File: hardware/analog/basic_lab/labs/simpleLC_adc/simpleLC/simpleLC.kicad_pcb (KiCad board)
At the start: 2 copper layers, 40.2 x 16.4 mm, 5 parts, among them J1 Conn_01x04_Male, J2 Conn_01x02_Male, Q2 BC547

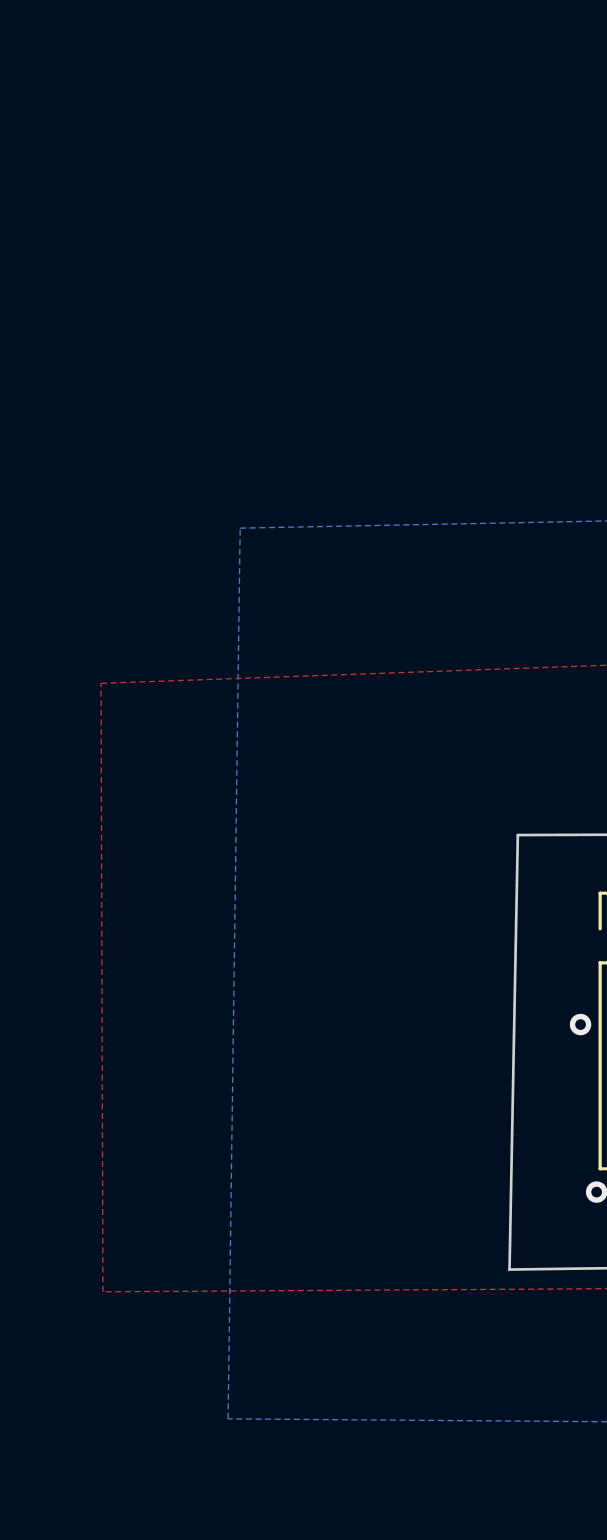
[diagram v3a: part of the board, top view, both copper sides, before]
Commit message: pwm => adc: started amplifier PCB
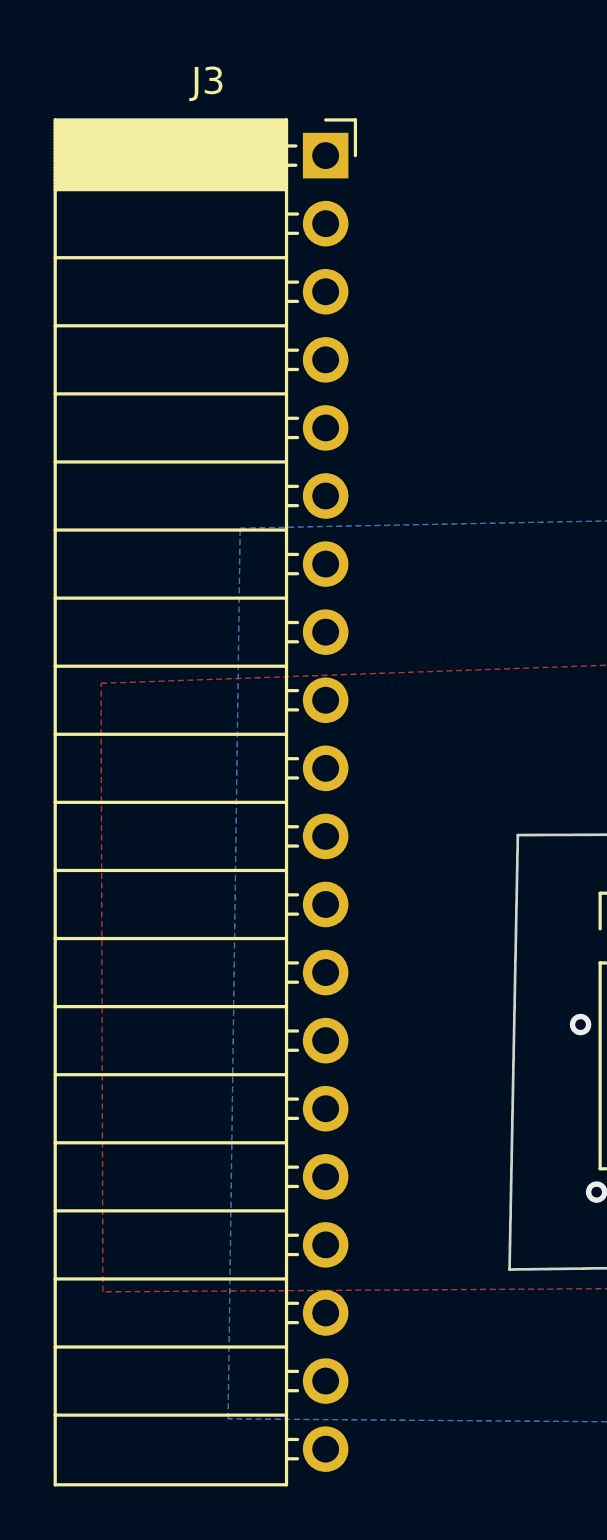
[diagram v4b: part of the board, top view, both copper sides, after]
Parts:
- added J3: Conn_01x20_Female, Connector_PinSocket_2.54mm:PinSocket_1x20_P2.54mm_Horizontal, F.Cu at (155.3, 60.8)

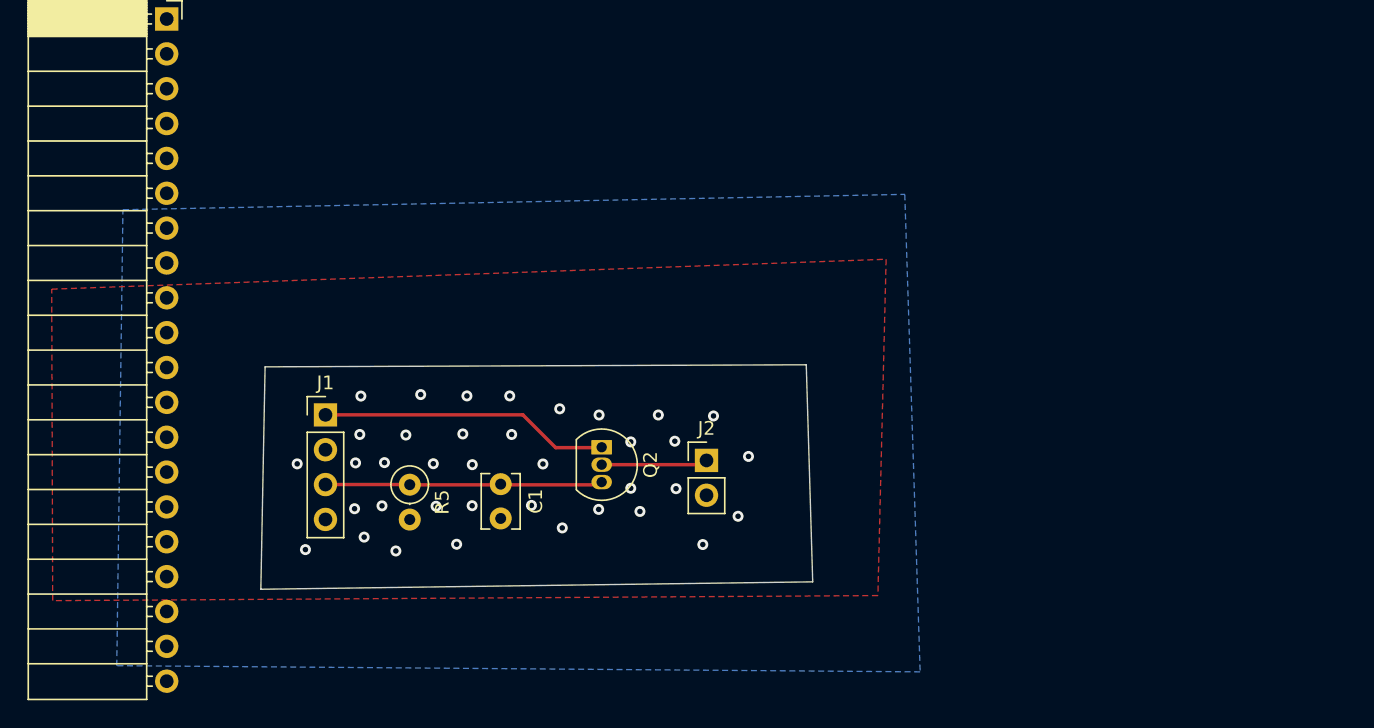
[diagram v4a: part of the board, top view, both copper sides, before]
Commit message: pwm => adc: started amplifier PCB
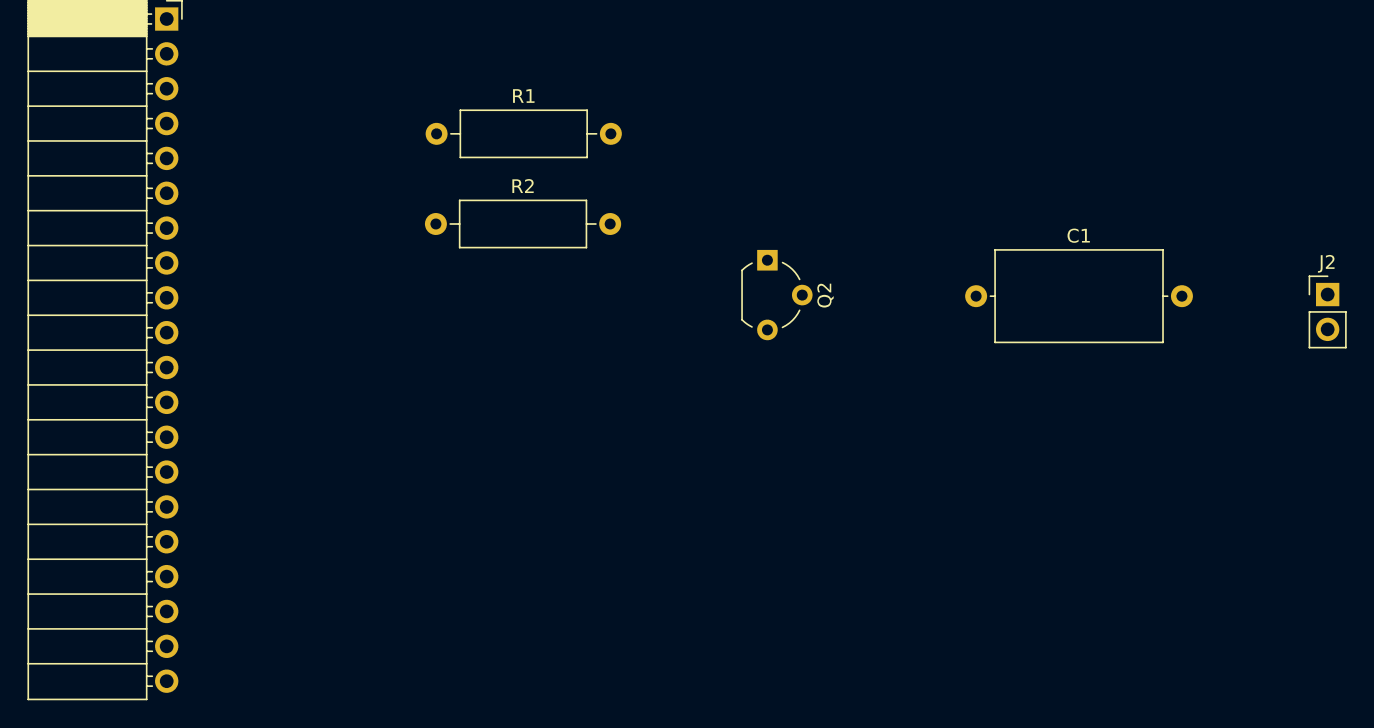
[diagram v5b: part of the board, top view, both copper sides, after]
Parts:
- removed J1: Conn_01x04_Male, Connector_PinHeader_2.54mm:PinHeader_1x04_P2.54mm_Vertical
- removed R5: R, Resistor_THT:R_Axial_DIN0207_L6.3mm_D2.5mm_P2.54mm_Vertical
- added R1: R, Resistor_THT:R_Axial_DIN0309_L9.0mm_D3.2mm_P12.70mm_Horizontal, F.Cu at (175.0, 69.2)
- added R2: R, Resistor_THT:R_Axial_DIN0309_L9.0mm_D3.2mm_P12.70mm_Horizontal, F.Cu at (175.0, 75.8)
- C1: footprint Capacitor_THT:C_Disc_D3.8mm_W2.6mm_P2.50mm -> Capacitor_THT:C_Axial_L12.0mm_D6.5mm_P15.00mm_Horizontal
- Q2: footprint Package_TO_SOT_THT:TO-92_Inline -> Package_TO_SOT_THT:TO-92_Wide
- moved J2 46.9 mm to (239.9, 80.9)
- moved C1 37.3 mm to (214.3, 81.0), turned to 0 degrees
- moved Q2 18.2 mm to (199.1, 78.4)
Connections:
- net Net-(J3-Pad11) renamed pwm
- C1 pad 1: aout -> Net-(C1-Pad1)
- C1 pad 2: GND -> Net-(C1-Pad2)
- J2 pad 1: Net-(J2-Pad1) -> Net-(C1-Pad2)
- J3 pad 12: Net-(J3-Pad12) -> adc
- J3 pad 18: Net-(J3-Pad18) -> GND
- J3 pad 19: Net-(J3-Pad19) -> +3V3
- J3 pad 20: Net-(J3-Pad20) -> GND
- Q2 pad 1: +3V3 -> adc
- Q2 pad 2: Net-(J2-Pad1) -> Net-(C1-Pad1)
- Q2 pad 3: aout -> GND
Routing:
- net +3V3: track 21.2 -> 0.00 mm
- net aout: track 20.2 -> 0.00 mm
- net Net-(J2-Pad1): track 7.84 -> 0.00 mm
- net GND: vias 37 -> 0
- removed copper zone on B.Cu, net GND
- removed copper zone on F.Cu, net GND
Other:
- board outline removed

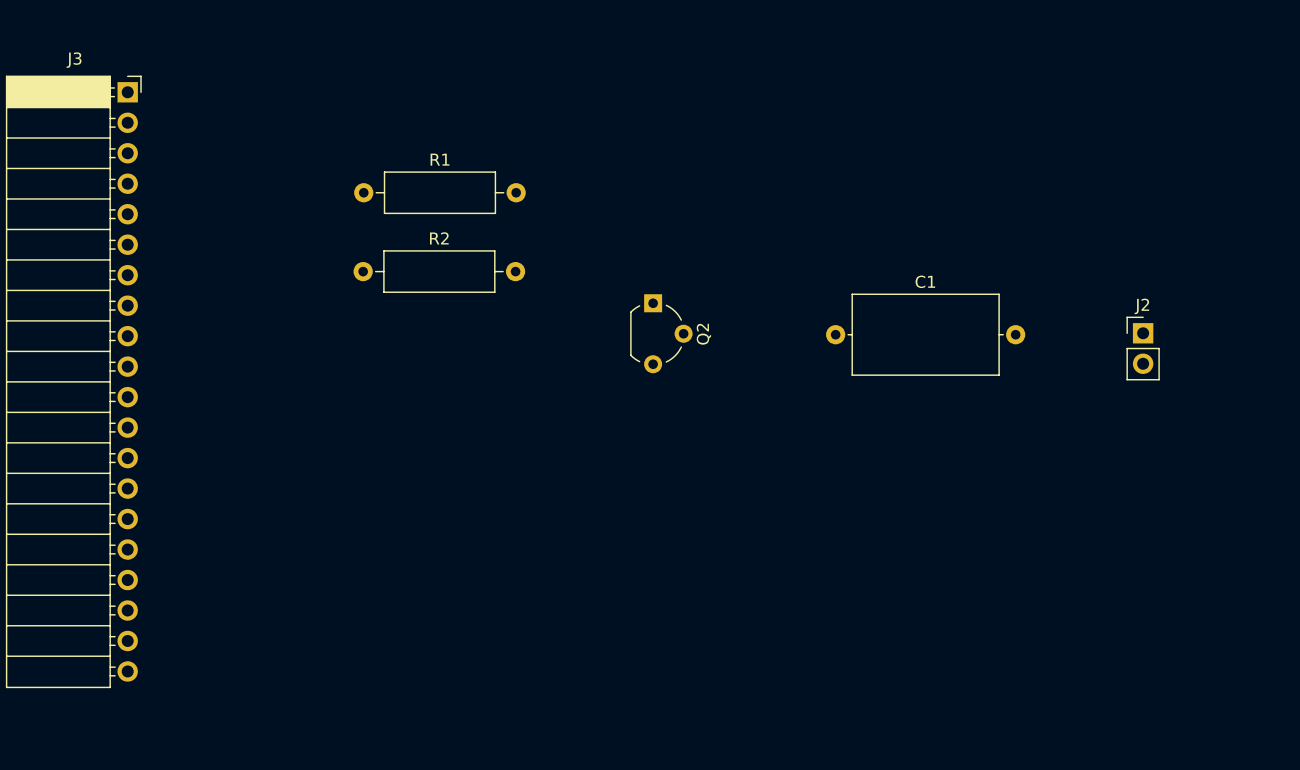
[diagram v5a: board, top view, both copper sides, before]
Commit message: pwm => adc: started amplifier PCB
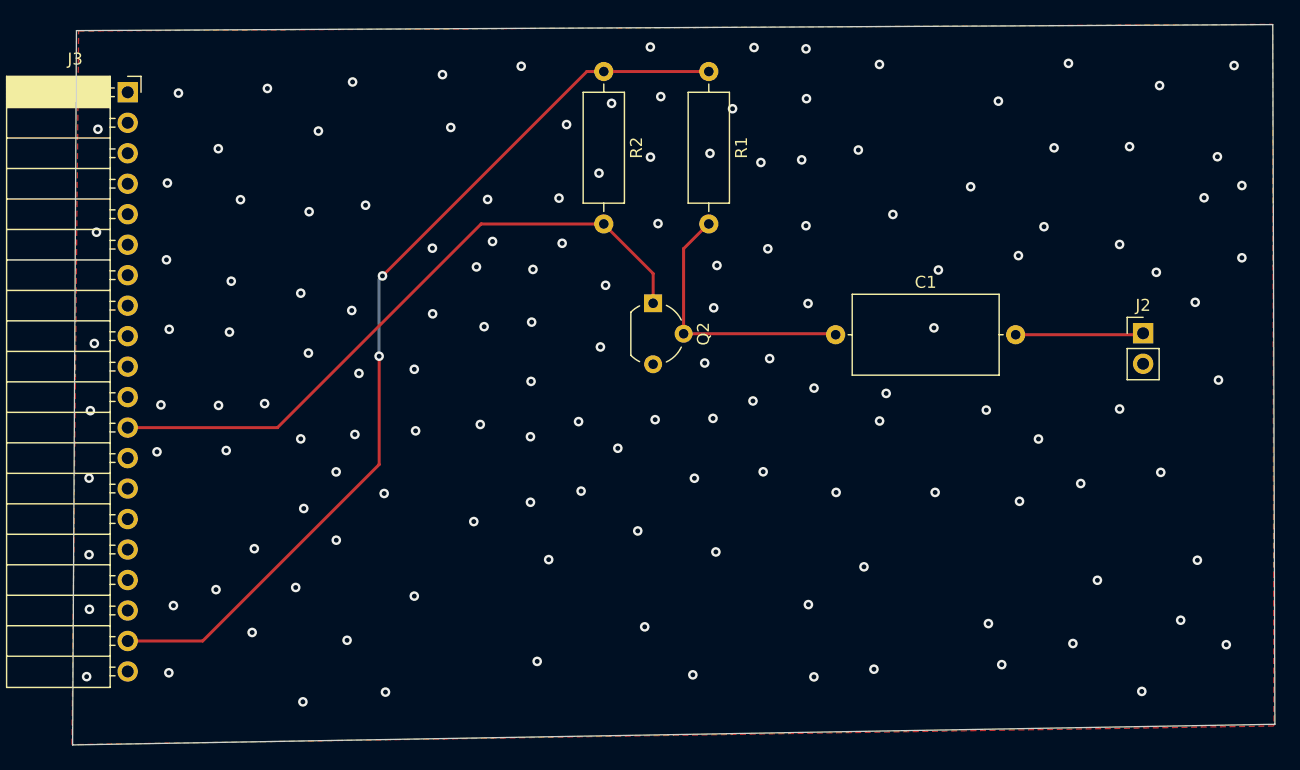
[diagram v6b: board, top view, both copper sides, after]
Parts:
- moved R1 30.5 mm to (203.8, 59.1), turned to 270 degrees
- moved R2 26.1 mm to (195.0, 59.1), turned to 270 degrees
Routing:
- net +3V3: track 0.00 -> 77.1 mm, vias 0 -> 2
- net adc: track 0.00 -> 55.0 mm
- net Net-(C1-Pad1): track 0.00 -> 22.6 mm
- net Net-(C1-Pad2): track 0.00 -> 10.6 mm
- net GND: vias 0 -> 148
- added copper zone on F.Cu, net GND
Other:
- board outline added: 100.2 x 60 mm

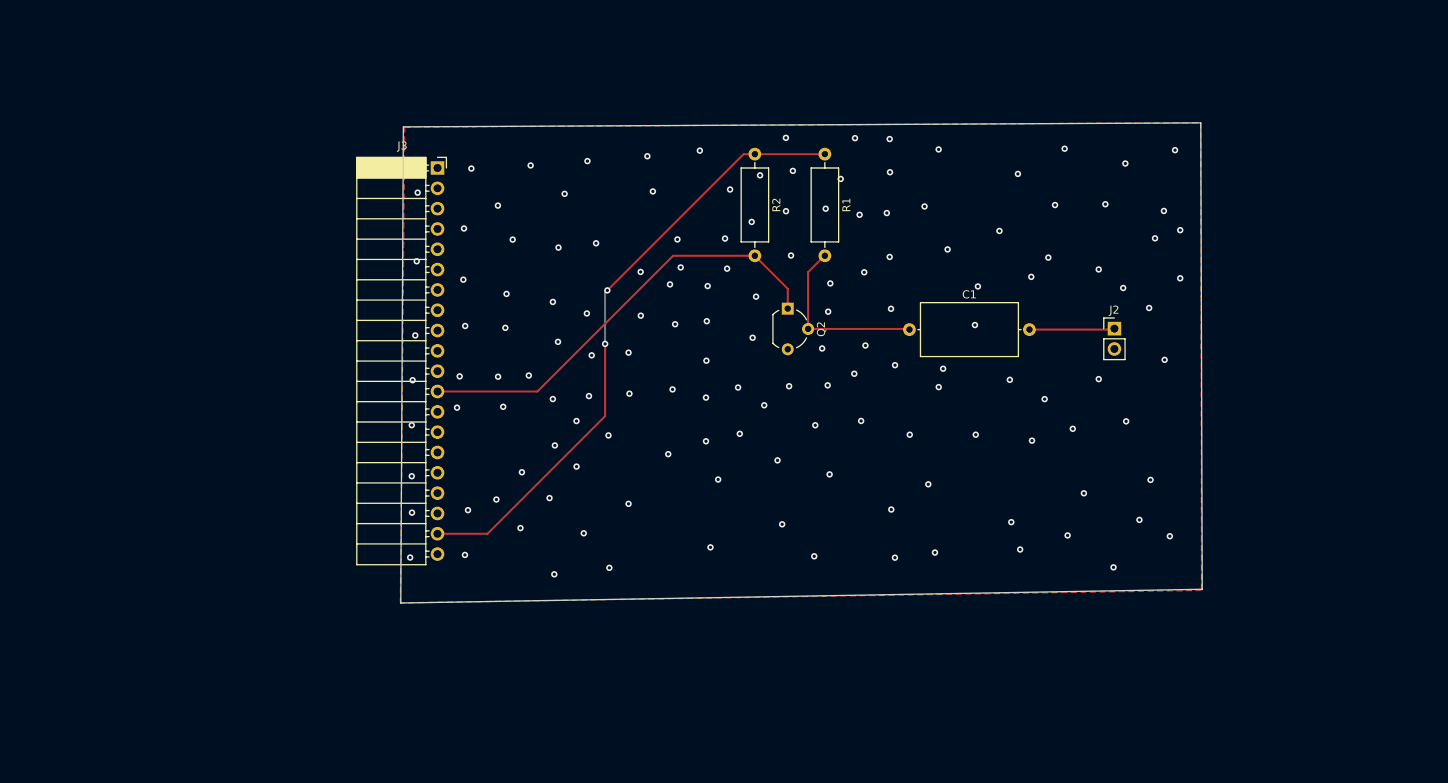
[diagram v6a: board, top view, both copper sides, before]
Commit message: pwm => adc: started amplifier PCB
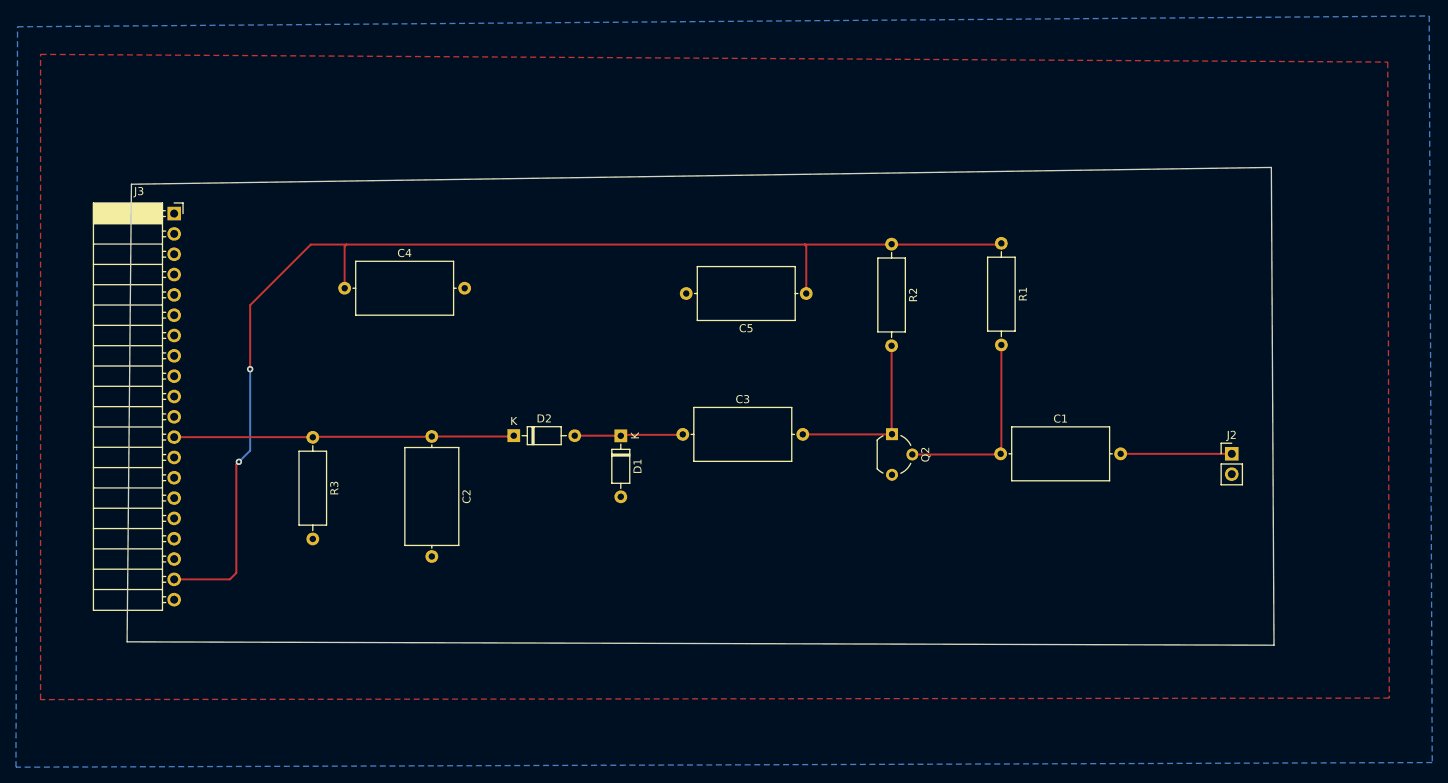
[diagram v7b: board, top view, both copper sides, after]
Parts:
- added C2: C, Capacitor_THT:C_Axial_L12.0mm_D6.5mm_P15.00mm_Horizontal, F.Cu at (154.6, 94.4)
- added C3: C, Capacitor_THT:C_Axial_L12.0mm_D6.5mm_P15.00mm_Horizontal, F.Cu at (186.0, 94.1)
- added C4: C, Capacitor_THT:C_Axial_L12.0mm_D6.5mm_P15.00mm_Horizontal, F.Cu at (143.7, 75.9)
- added C5: C, Capacitor_THT:C_Axial_L12.0mm_D6.5mm_P15.00mm_Horizontal, F.Cu at (201.4, 76.5)
- added D1: 1N4148, Diode_THT:D_DO-35_SOD27_P7.62mm_Horizontal, F.Cu at (178.2, 94.3)
- added D2: 1N4148, Diode_THT:D_DO-35_SOD27_P7.62mm_Horizontal, F.Cu at (164.9, 94.3)
- added R3: R, Resistor_THT:R_Axial_DIN0309_L9.0mm_D3.2mm_P12.70mm_Horizontal, F.Cu at (139.8, 94.5)
- moved J3 33.4 mm to (122.4, 66.5)
- moved R1 24.7 mm to (225.8, 70.2)
- moved J2 21.5 mm to (254.6, 96.6)
- moved R2 20.5 mm to (212.1, 70.3)
- moved Q2 20.4 mm to (212.2, 94.1)
- moved C1 19.3 mm to (225.7, 96.6)
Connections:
- Q2 pad 1: adc -> Net-(C3-Pad2)
- R2 pad 2: adc -> Net-(C3-Pad2)
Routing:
- net +3V3: track 77.1 -> 151.0 mm
- net Net-(C3-Pad2): track 0.00 -> 22.7 mm
- net det: track 0.00 -> 13.5 mm
- net adc: track 55.0 -> 42.5 mm
- net Net-(C1-Pad2): track 10.6 -> 14.1 mm
- net Net-(C1-Pad1): track 22.6 -> 24.5 mm
- net GND: vias 148 -> 0
- added copper zone on B.Cu, net GND
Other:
- board size 100.2 x 60 mm -> 143.4 x 59.7 mm
